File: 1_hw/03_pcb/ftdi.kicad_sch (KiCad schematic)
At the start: 34 parts, among them Y3 12 MHz

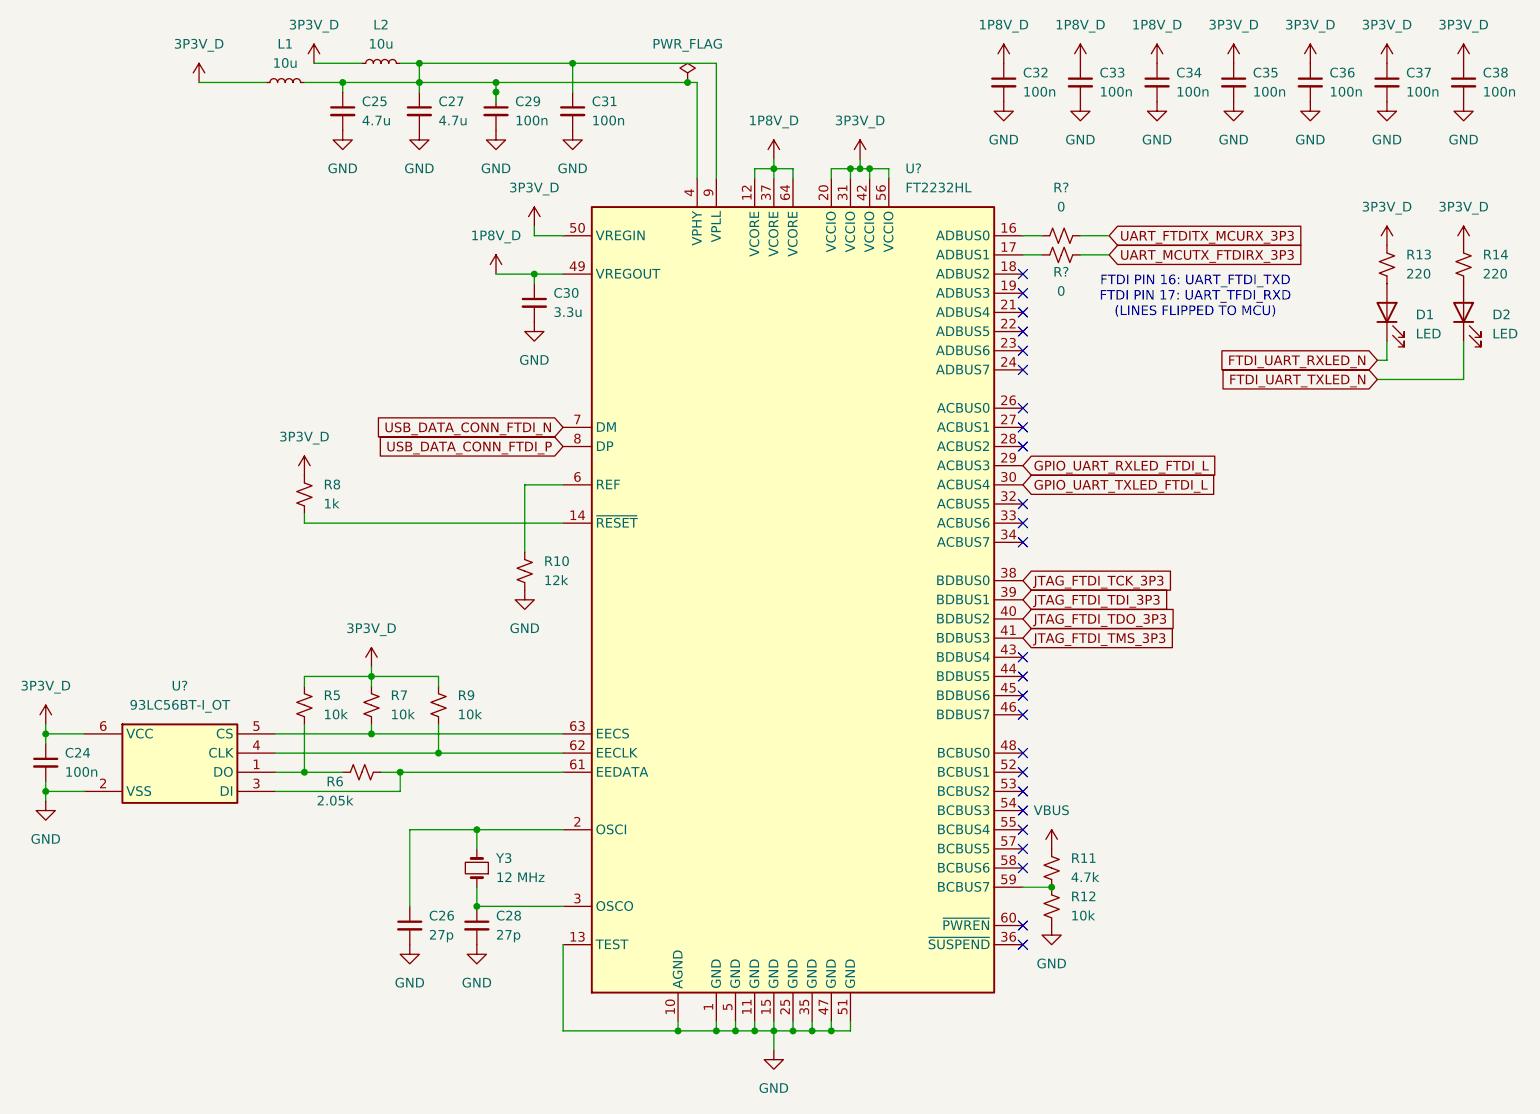
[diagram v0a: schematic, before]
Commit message: FEAT: Added Connectors on Schematic. Created Connector Footprints.
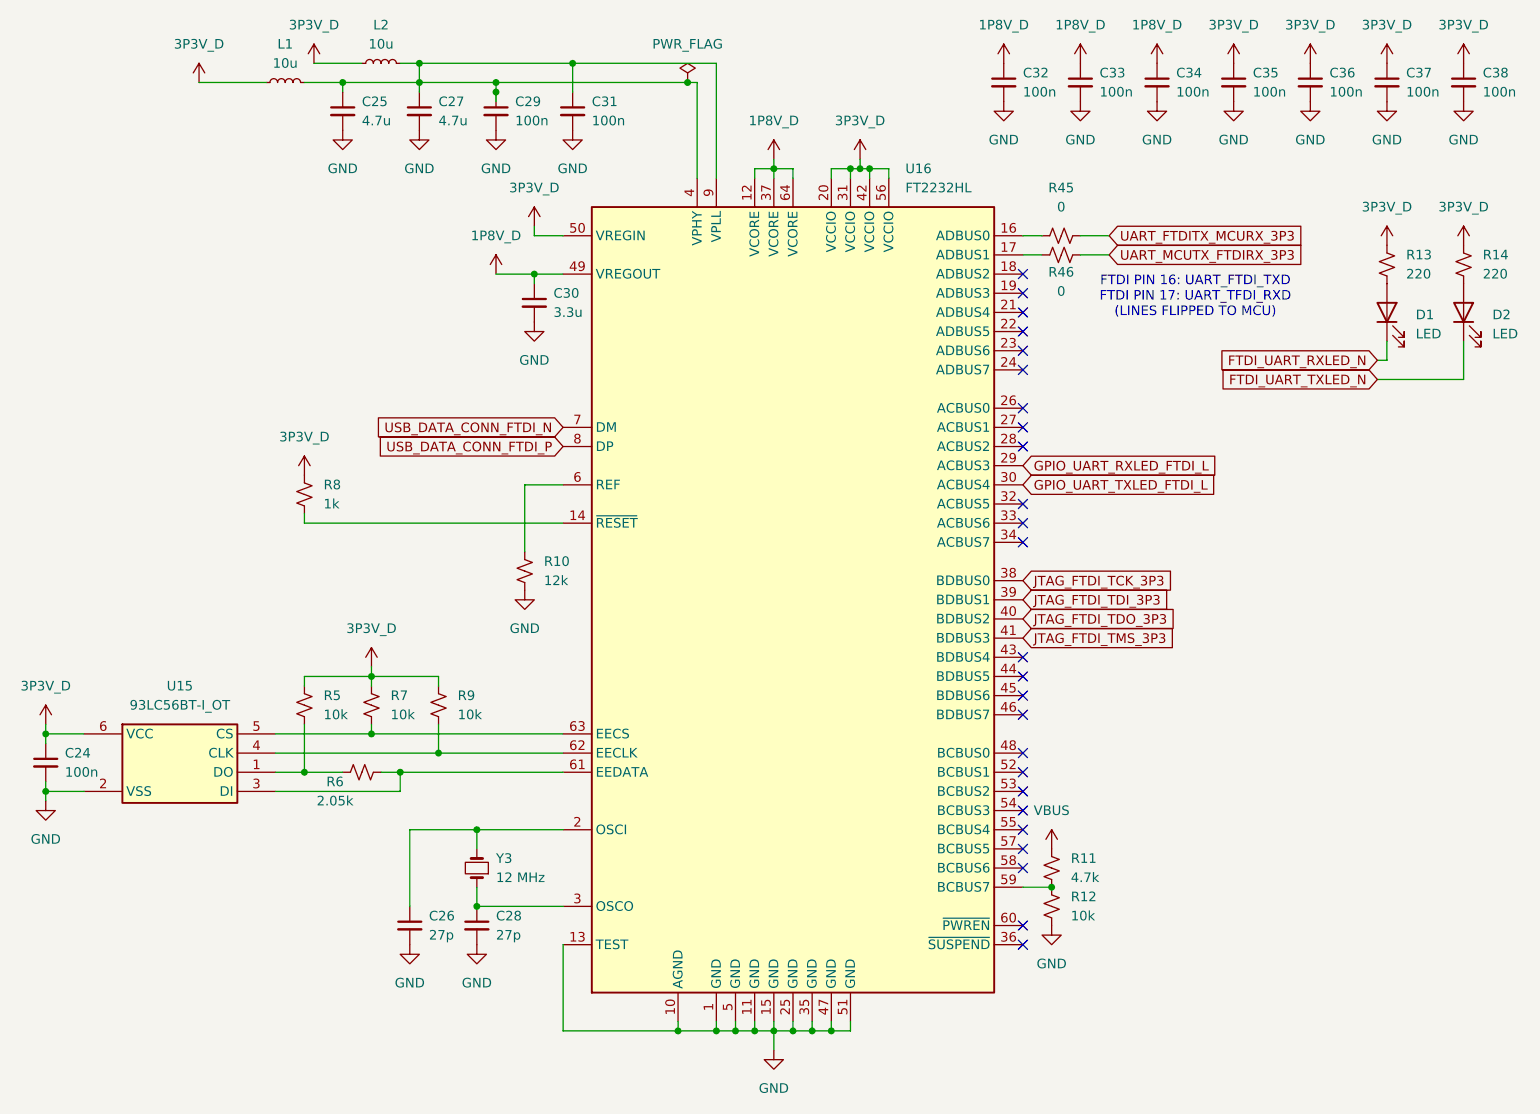
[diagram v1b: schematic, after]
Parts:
- gave numbers to parts that had none: 4
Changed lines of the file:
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@@
 		(dnp no)
 		(fields_autoplaced yes)
-		(property "Reference" "U?"
+		(property "Reference" "U15"
 			(at 71.12 114.3 0)
 			(effects
@@
 			(project ""
 				(path "/866ef9be-3b01-4288-a6e0-a2357aa17e50/671babe9-63c4-471b-b226-781a2641e7ad"
-					(reference "U?")
+					(reference "U15")
 					(unit 1)
 				)
@@
 		(dnp no)
 		(fields_autoplaced yes)
-		(property "Reference" "U?"
+		(property "Reference" "U16"
 			(at 167.2941 45.72 0)
 			(effects
@@
 			(project ""
 				(path "/866ef9be-3b01-4288-a6e0-a2357aa17e50/671babe9-63c4-471b-b226-781a2641e7ad"
-					(reference "U?")
+					(reference "U16")
 					(unit 1)
 				)
@@
 		(dnp no)
 		(fields_autoplaced yes)
-		(property "Reference" "R?"
+		(property "Reference" "R45"
 			(at 187.96 48.26 90)
 			(effects
@@
 			(project "arb"
 				(path "/866ef9be-3b01-4288-a6e0-a2357aa17e50/671babe9-63c4-471b-b226-781a2641e7ad"
-					(reference "R?")
+					(reference "R45")
 					(unit 1)
 				)
@@
 		(on_board yes)
 		(dnp no)
-		(property "Reference" "R?"
+		(property "Reference" "R46"
 			(at 187.96 59.436 90)
 			(effects
@@
 			(project "arb"
 				(path "/866ef9be-3b01-4288-a6e0-a2357aa17e50/671babe9-63c4-471b-b226-781a2641e7ad"
-					(reference "R?")
+					(reference "R46")
 					(unit 1)
 				)

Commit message: FEAT: Assigned Reference Designators; Assigned Passives Part Numbers & Footprints (0603); Assigned LCSC P/Ns.
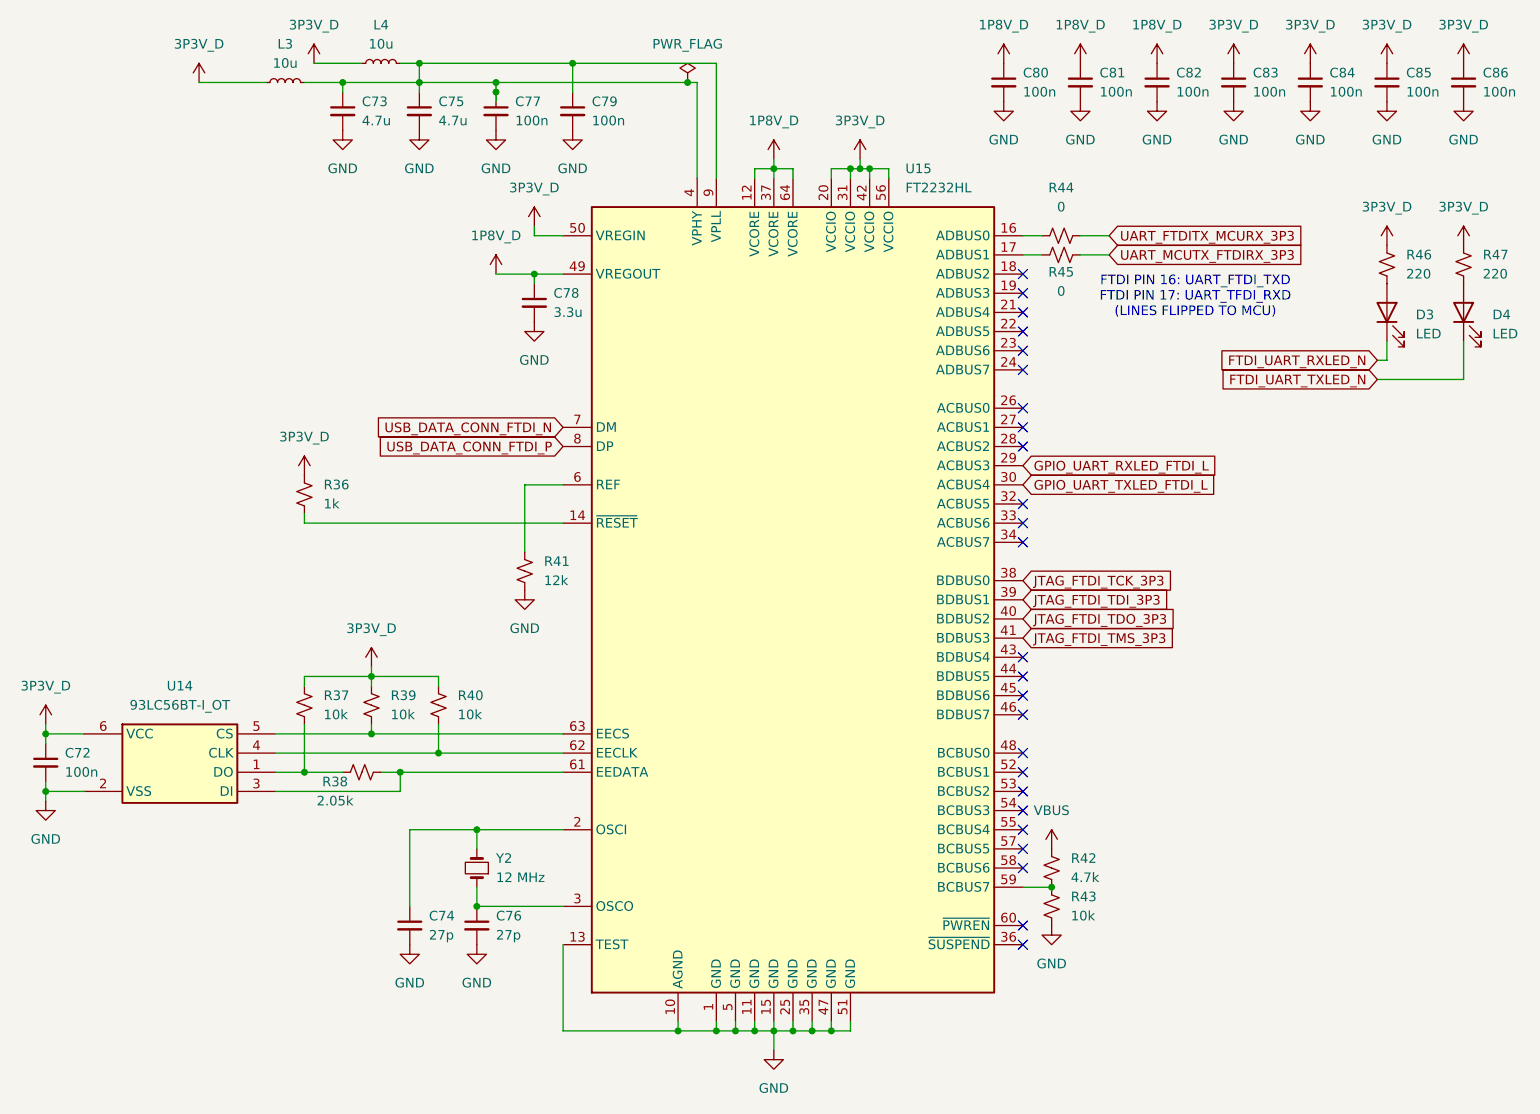
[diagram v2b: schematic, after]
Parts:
- C72: renamed from C24; LCSC (none) -> C24452; PN CL10B104JB8NNNC -> (none); Part Number (none) -> CL10B104JB8NNNC
- C73: renamed from C25; LCSC (none) -> C1705; PN CC0603KRX5R5BB475 -> (none); Part Number (none) -> CL10A475KP8NNNC
- C74: renamed from C26; LCSC (none) -> C1656; PN CC0603GRNPO0BN270 -> (none); Part Number (none) -> CL10C270JB8NNNC
- C75: renamed from C27; LCSC (none) -> C1705; PN CC0603KRX5R5BB475 -> (none); Part Number (none) -> CL10A475KP8NNNC
- C76: renamed from C28; LCSC (none) -> C1656; PN CC0603GRNPO0BN270 -> (none); Part Number (none) -> CL10C270JB8NNNC
- C77: renamed from C29; LCSC (none) -> C24452; PN CL10B104JB8NNNC -> (none); Part Number (none) -> CL10B104JB8NNNC
- C78: renamed from C30; LCSC (none) -> C51412; PN GRM188R61A335KE15D -> (none); Part Number (none) -> CL10A335KP8NNNC
- C79: renamed from C31; LCSC (none) -> C24452; PN CL10B104JB8NNNC -> (none); Part Number (none) -> CL10B104JB8NNNC
- C80: renamed from C32; LCSC (none) -> C24452; PN CL10B104JB8NNNC -> (none); Part Number (none) -> CL10B104JB8NNNC
- C81: renamed from C33; LCSC (none) -> C24452; PN CL10B104JB8NNNC -> (none); Part Number (none) -> CL10B104JB8NNNC
- C82: renamed from C34; LCSC (none) -> C24452; PN CL10B104JB8NNNC -> (none); Part Number (none) -> CL10B104JB8NNNC
- C83: renamed from C35; LCSC (none) -> C24452; PN CL10B104JB8NNNC -> (none); Part Number (none) -> CL10B104JB8NNNC
- C84: renamed from C36; LCSC (none) -> C24452; PN CL10B104JB8NNNC -> (none); Part Number (none) -> CL10B104JB8NNNC
- C85: renamed from C37; LCSC (none) -> C24452; PN CL10B104JB8NNNC -> (none); Part Number (none) -> CL10B104JB8NNNC
- C86: renamed from C38; LCSC (none) -> C24452; PN CL10B104JB8NNNC -> (none); Part Number (none) -> CL10B104JB8NNNC
- D3: renamed from D1; LCSC (none) -> C7496845; PN F.1206.00003/P2-1206R1TS2-09T-001 -> (none); Part Number (none) -> F.1206.00003/P2-1206R1TS2-09T-001
- D4: renamed from D2; LCSC (none) -> C7496845; PN F.1206.00003/P2-1206R1TS2-09T-001 -> (none); Part Number (none) -> F.1206.00003/P2-1206R1TS2-09T-001
- L3: renamed from L1; LCSC (none) -> C373750; PN LS0603-100J-N -> (none); Part Number (none) -> LS0603-100J-N
- L4: renamed from L2; LCSC (none) -> C373750; PN LS0603-100J-N -> (none); Part Number (none) -> LS0603-100J-N
- R36: renamed from R8; LCSC (none) -> C22548; PN RC0603JR-071KL -> (none); Part Number (none) -> RC0603FR-071KL
- R37: renamed from R5; LCSC (none) -> C25804; PN CR-03FC7---10K -> (none); Part Number (none) -> 0603WAF1002T5E
- R38: renamed from R6; LCSC (none) -> C22900; PN RT0603DRE072K05L -> (none); Part Number (none) -> 0603WAF2051T5E
- R39: renamed from R7; LCSC (none) -> C25804; PN CR-03FC7---10K -> (none); Part Number (none) -> 0603WAF1002T5E
- R40: renamed from R9; LCSC (none) -> C25804; PN CR-03FC7---10K -> (none); Part Number (none) -> 0603WAF1002T5E
- R41: renamed from R10; LCSC (none) -> C22790; PN RT0603DRD0712KL -> (none); Part Number (none) -> 0603WAF1202T5E
- R42: renamed from R11; LCSC (none) -> C99782; PN RT0603DRD074K7L -> (none); Part Number (none) -> RC0603FR-074K7L
- R43: renamed from R12; LCSC (none) -> C25804; PN CR-03FC7---10K -> (none); Part Number (none) -> 0603WAF1002T5E
- R44: renamed from R45; LCSC (none) -> C15402; PN 0603WAJ0000T5E -> (none); Part Number (none) -> 0603WAJ0000T5E
- R45: renamed from R46; LCSC (none) -> C15402; PN 0603WAJ0000T5E -> (none); Part Number (none) -> 0603WAJ0000T5E
- R46: renamed from R13; LCSC (none) -> C22962; PN ESR03EZPJ221 -> (none); Part Number (none) -> 0603WAF2200T5E
- R47: renamed from R14; LCSC (none) -> C22962; PN ESR03EZPJ221 -> (none); Part Number (none) -> 0603WAF2200T5E
- U14: renamed from U15; LCSC (none) -> C190271
- U15: renamed from U16; LCSC (none) -> C27882
- Y2: renamed from Y3; LCSC (none) -> C9002; PN X322512MSB4SI -> (none); Part Number (none) -> X322512MSB4SI

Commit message: FEAT: Added MCU Flash. Finished creating & assigning footprints. Ran ERC & cleared out issues. Ready for Layout.
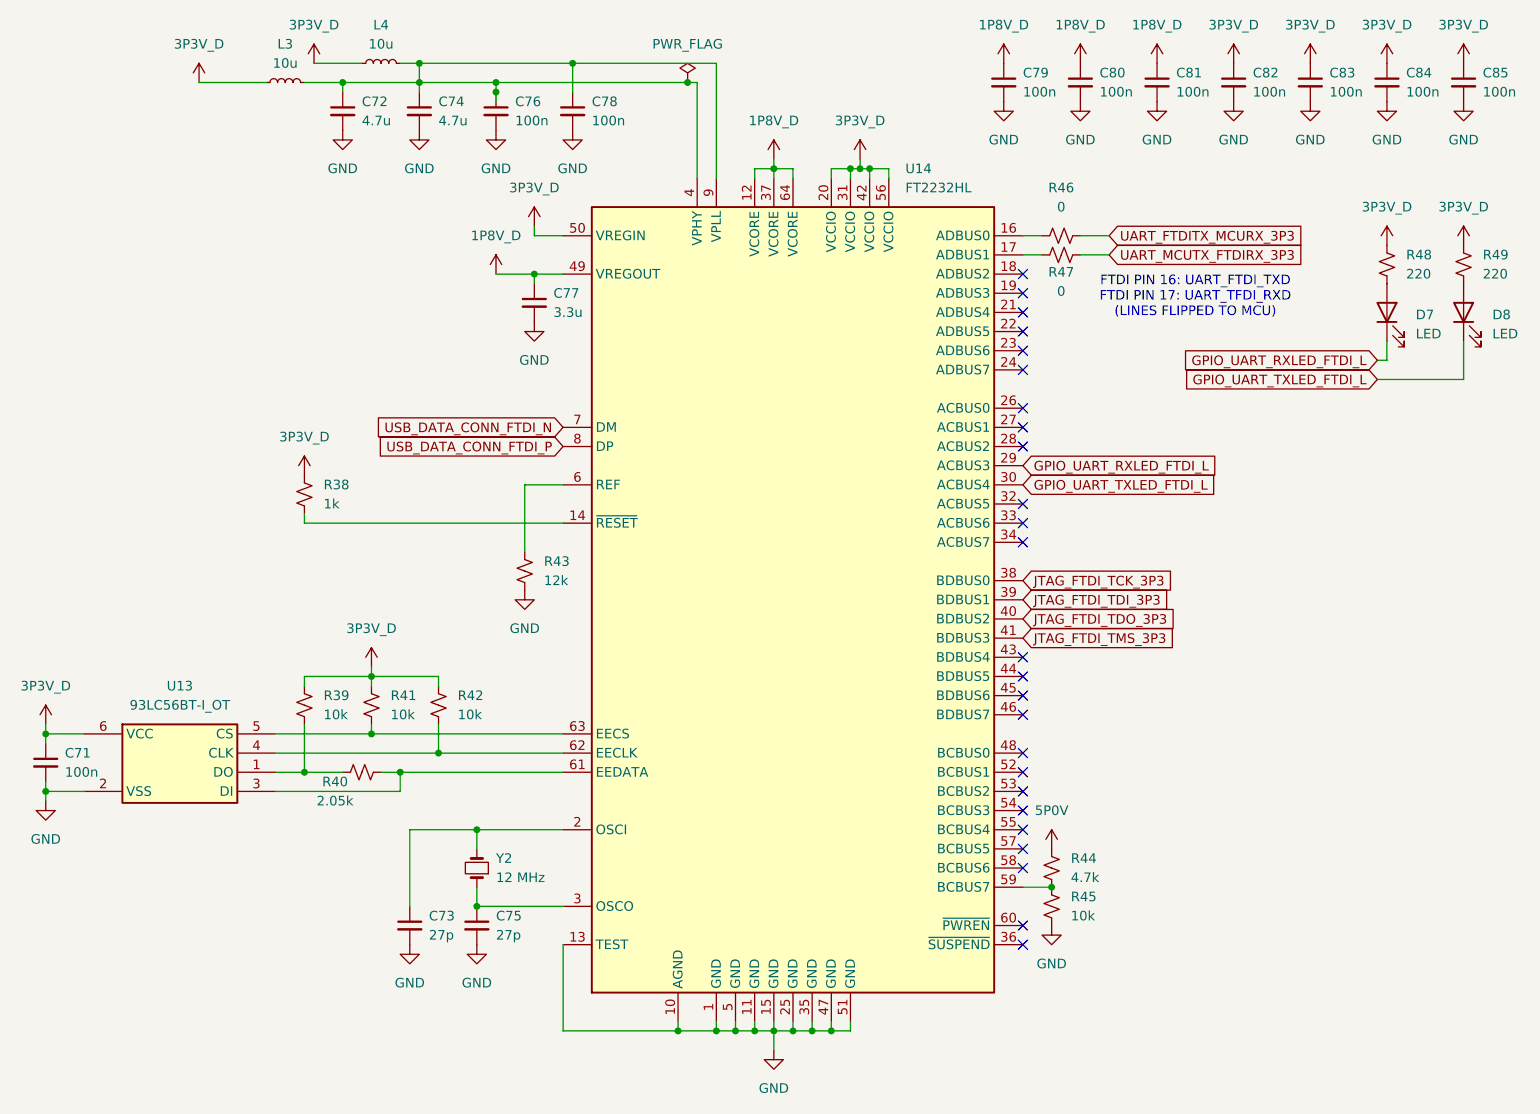
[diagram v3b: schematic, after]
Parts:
- U13: renamed from U14; footprint SOT95P270X145-6N -> Package_TO_SOT_SMD:SOT-23-6
- renumbered C72 to C71, C73 to C72, C74 to C73, C75 to C74, C76 to C75, C77 to C76, C78 to C77, C79 to C78, C80 to C79, C81 to C80, C82 to C81, C83 to C82, C84 to C83, C85 to C84, C86 to C85, D3 to D7, D4 to D8, R36 to R38, R37 to R39, R38 to R40, R39 to R41, R40 to R42, R41 to R43, R42 to R44, R43 to R45, R44 to R46, R45 to R47, R46 to R48, R47 to R49, U15 to U14
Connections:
- net FTDI_UART_RXLED_N is gone; now on net GPIO_UART_RXLED_FTDI_L: D7.1 (K)
- net FTDI_UART_TXLED_N is gone; now on net GPIO_UART_TXLED_FTDI_L: D8.1 (K)
- net VBUS renamed 5P0V
